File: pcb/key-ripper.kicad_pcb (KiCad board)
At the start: 2 copper layers, 290.5 x 121.4 mm, 193 parts, among them J1 Conn_01x04, SW1 ESC, SW10 F9, SW11 F10, SW12 F11, SW13 F12, SW14 TILDE, SW15 1, SW16 2, SW17 3, SW18 4, SW19 5, SW2 F1, SW20 6, SW21 7, SW22 8, SW23 9, SW24 0, SW25 -, SW26 +, SW27 BACKSPACE, SW28 TAB, SW29 Q, SW3 F2, SW30 W, SW31 E, SW32 R, SW33 T, SW34 Y, SW35 U, SW36 I, SW37 O, SW38 P, SW39 [, SW4 F3, SW40 ], SW41 BACKSLASH, SW42 CAPS, SW43 A, SW44 S, SW45 D, SW46 F, SW47 G, SW48 H, SW49 J, SW5 F4, SW50 K, SW51 L, SW52 ;, SW53 ', SW54 ENTER, SW55 L_SHIFT, SW56 Z, SW57 X, SW58 C, SW59 V, SW6 F5, SW60 B, SW61 N, SW62 M, SW63 ,, SW64 ., SW65 FWD_SLASH, SW66 UP, SW67 FN, SW68 BL_CTRL, SW69 L_ALT, SW7 F6, SW70 L_CMD, SW71 SPACE, SW72 R_CMD, SW73 LEFT, SW74 DOWN, SW75 RIGHT, SW8 F7, SW9 F8, U1 RP2040, U2 TYPE-C-31-M-12, U3 XC6206PxxxMR, U4 W25Q128JVS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

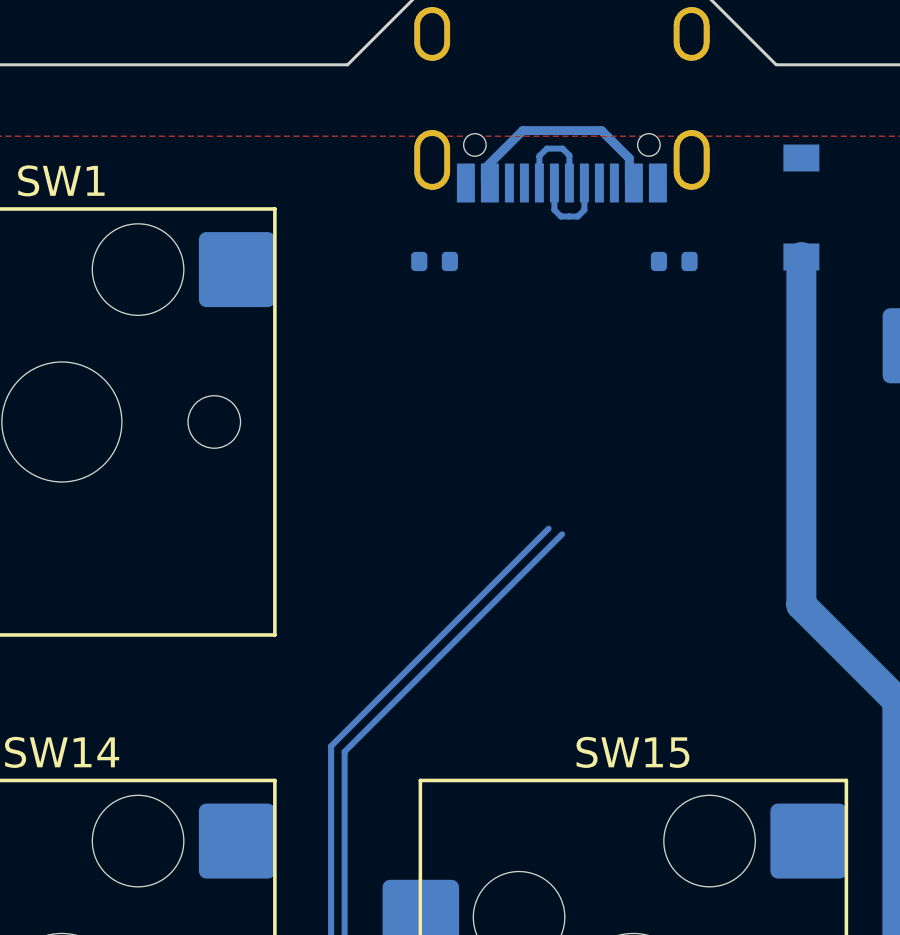
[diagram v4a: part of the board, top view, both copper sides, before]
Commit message: Reattach USB C differential pair
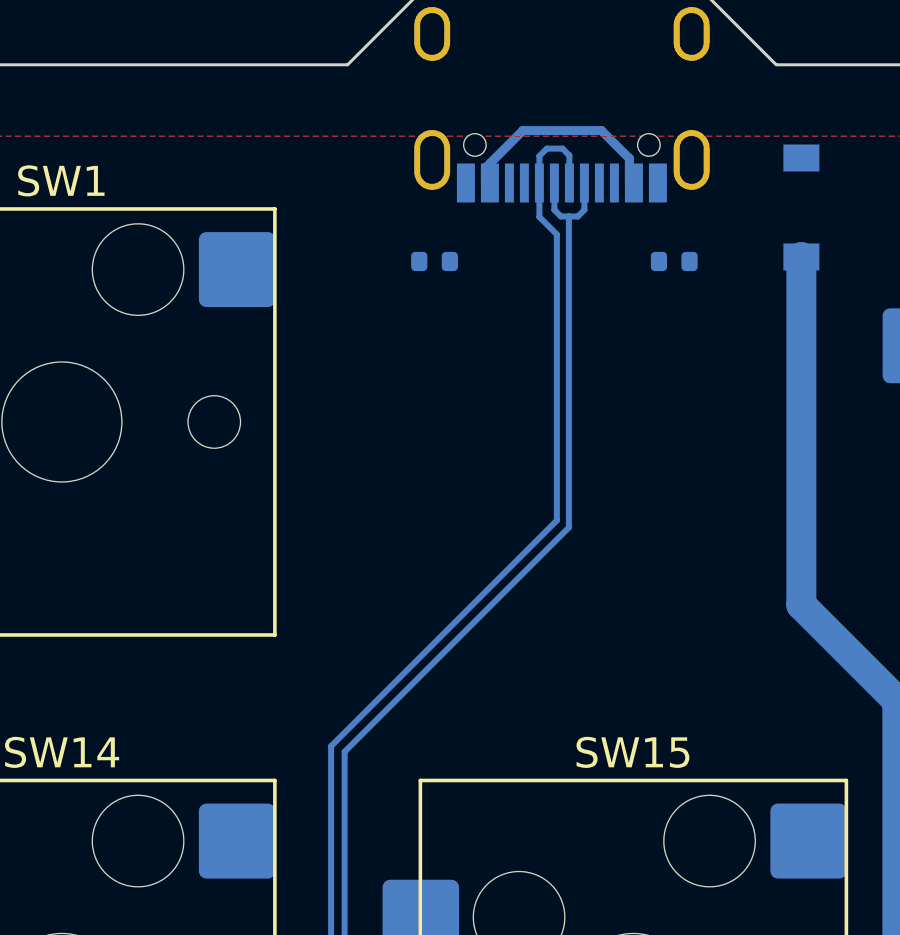
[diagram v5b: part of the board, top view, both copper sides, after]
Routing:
- net USB-: track 173.8 -> 185.6 mm
- net USB+: track 172.8 -> 183.5 mm
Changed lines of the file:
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@@
   (segment (start 18.91767 -27.83233) (end 18.91767 -27.015913) (width 0.3) (layer "B.Cu") (net 94))
   (segment (start 17.417797 -26.117018) (end 17.200779 -25.9) (width 0.2) (layer "B.Cu") (net 100))
+  (segment (start 12.0932 11.225) (end 15.8432 11.225) (width 0.2) (layer "B.Cu") (net 100))
+  (segment (start 16.9 -25.9) (end 16.9 -15.5318) (width 0.2) (layer "B.Cu") (net 100))
+  (segment (start 15.8432 11.225) (end 17.525 12.9068) (width 0.2) (layer "B.Cu") (net 100))
+  (segment (start 9.425 8.5568) (end 12.0932 11.225) (width 0.2) (layer "B.Cu") (net 100))
+  (segment (start 16.9 -15.5318) (end 9.425 -8.0568) (width 0.2) (layer "B.Cu") (net 100))
+  (segment (start 31.1432 47.525) (end 31.675 48.0568) (width 0.2) (layer "B.Cu") (net 100))
   (segment (start 17.525 12.9068) (end 17.525 46.6068) (width 0.2) (layer "B.Cu") (net 100))
-  (segment (start 35.1432 67.875) (end 67.7432 67.875) (width 0.2) (layer "B.Cu") (net 100))
+  (segment (start 17.200779 -25.9) (end 16.9 -25.9) (width 0.2) (layer "B.Cu") (net 100))
   (segment (start 31.675 64.4068) (end 35.1432 67.875) (width 0.2) (layer "B.Cu") (net 100))
-  (segment (start 31.675 48.0568) (end 31.675 64.4068) (width 0.2) (layer "B.Cu") (net 100))
-  (segment (start 12.0932 11.225) (end 15.8432 11.225) (width 0.2) (layer "B.Cu") (net 100))
-  (segment (start 18.4432 47.525) (end 31.1432 47.525) (width 0.2) (layer "B.Cu") (net 100))
-  (segment (start 17.200779 -25.9) (end 16.9 -25.9) (width 0.2) (layer "B.Cu") (net 100))
-  (segment (start 31.1432 47.525) (end 31.675 48.0568) (width 0.2) (layer "B.Cu") (net 100))
-  (segment (start 67.7432 67.875) (end 77.343199 77.474999) (width 0.2) (layer "B.Cu") (net 100))
   (segment (start 94.115001 77.474999) (end 94.39 77.2) (width 0.2) (layer "B.Cu") (net 100))
   (segment (start 16.417797 -26.116764) (end 16.417797 -27.015913) (width 0.2) (layer "B.Cu") (net 100))
-  (segment (start 16.675 -15.3068) (end 9.425 -8.0568) (width 0.2) (layer "B.Cu") (net 100))
-  (segment (start 9.425 8.5568) (end 12.0932 11.225) (width 0.2) (layer "B.Cu") (net 100))
+  (segment (start 9.425 -8.0568) (end 9.425 8.5568) (width 0.2) (layer "B.Cu") (net 100))
+  (segment (start 31.675 48.0568) (end 31.675 64.4068) (width 0.2) (layer "B.Cu") (net 100))
   (segment (start 16.9 -25.9) (end 16.634561 -25.9) (width 0.2) (layer "B.Cu") (net 100))
+  (segment (start 18.4432 47.525) (end 31.1432 47.525) (width 0.2) (layer "B.Cu") (net 100))
   (segment (start 77.343199 77.474999) (end 94.115001 77.474999) (width 0.2) (layer "B.Cu") (net 100))
-  (segment (start 17.525 46.6068) (end 18.4432 47.525) (width 0.2) (layer "B.Cu") (net 100))
-  (segment (start 15.8432 11.225) (end 17.525 12.9068) (width 0.2) (layer "B.Cu") (net 100))
-  (segment (start 9.425 -8.0568) (end 9.425 8.5568) (width 0.2) (layer "B.Cu") (net 100))
+  (segment (start 67.7432 67.875) (end 77.343199 77.474999) (width 0.2) (layer "B.Cu") (net 100))
+  (segment (start 35.1432 67.875) (end 67.7432 67.875) (width 0.2) (layer "B.Cu") (net 100))
   (segment (start 16.634561 -25.9) (end 16.417797 -26.116764) (width 0.2) (layer "B.Cu") (net 100))
   (segment (start 17.417797 -27.015913) (end 17.417797 -26.117018) (width 0.2) (layer "B.Cu") (net 100))
+  (segment (start 17.525 46.6068) (end 18.4432 47.525) (width 0.2) (layer "B.Cu") (net 100))
+  (segment (start 17.075 46.7932) (end 18.2568 47.975) (width 0.2) (layer "B.Cu") (net 101))
   (segment (start 16.6875 -28.1625) (end 16.91767 -27.93233) (width 0.2) (layer "B.Cu") (net 101))
+  (segment (start 16.165362 -28.1625) (end 16.6875 -28.1625) (width 0.2) (layer "B.Cu") (net 101))
+  (segment (start 15.91767 -27.015913) (end 15.91767 -25.88233) (width 0.2) (layer "B.Cu") (net 101))
+  (segment (start 30.9568 47.975) (end 31.225 48.2432) (width 0.2) (layer "B.Cu") (net 101))
+  (segment (start 15.91767 -25.88233) (end 16.5 -25.3) (width 0.2) (layer "B.Cu") (net 101))
+  (segment (start 94.115001 77.925001) (end 94.39 78.2) (width 0.2) (layer "B.Cu") (net 101))
+  (segment (start 16.91767 -27.93233) (end 16.91767 -27.015913) (width 0.2) (layer "B.Cu") (net 101))
+  (segment (start 31.225 64.5932) (end 34.9568 68.325) (width 0.2) (layer "B.Cu") (net 101))
+  (segment (start 77.156801 77.925001) (end 94.115001 77.925001) (width 0.2) (layer "B.Cu") (net 101))
+  (segment (start 16.5 -15.7682) (end 8.975 -8.2432) (width 0.2) (layer "B.Cu") (net 101))
+  (segment (start 34.9568 68.325) (end 67.5568 68.325) (width 0.2) (layer "B.Cu") (net 101))
+  (segment (start 15.91767 -27.914808) (end 16.165362 -28.1625) (width 0.2) (layer "B.Cu") (net 101))
+  (segment (start 67.5568 68.325) (end 77.156801 77.925001) (width 0.2) (layer "B.Cu") (net 101))
   (segment (start 8.975 8.7432) (end 11.9068 11.675) (width 0.2) (layer "B.Cu") (net 101))
-  (segment (start 16.165362 -28.1625) (end 16.6875 -28.1625) (width 0.2) (layer "B.Cu") (net 101))
+  (segment (start 11.9068 11.675) (end 15.6568 11.675) (width 0.2) (layer "B.Cu") (net 101))
+  (segment (start 15.6568 11.675) (end 17.075 13.0932) (width 0.2) (layer "B.Cu") (net 101))
+  (segment (start 15.91767 -27.015913) (end 15.91767 -27.914808) (width 0.2) (layer "B.Cu") (net 101))
   (segment (start 31.225 48.2432) (end 31.225 64.5932) (width 0.2) (layer "B.Cu") (net 101))
-  (segment (start 16.225 -15.4932) (end 8.975 -8.2432) (width 0.2) (layer "B.Cu") (net 101))
-  (segment (start 16.91767 -27.93233) (end 16.91767 -27.015913) (width 0.2) (layer "B.Cu") (net 101))
+  (segment (start 18.2568 47.975) (end 30.9568 47.975) (width 0.2) (layer "B.Cu") (net 101))
   (segment (start 17.075 13.0932) (end 17.075 46.7932) (width 0.2) (layer "B.Cu") (net 101))
-  (segment (start 11.9068 11.675) (end 15.6568 11.675) (width 0.2) (layer "B.Cu") (net 101))
-  (segment (start 15.91767 -27.914808) (end 16.165362 -28.1625) (width 0.2) (layer "B.Cu") (net 101))
-  (segment (start 15.6568 11.675) (end 17.075 13.0932) (width 0.2) (layer "B.Cu") (net 101))
+  (segment (start 16.5 -25.3) (end 16.5 -15.7682) (width 0.2) (layer "B.Cu") (net 101))
   (segment (start 8.975 -8.2432) (end 8.975 8.7432) (width 0.2) (layer "B.Cu") (net 101))
-  (segment (start 17.075 46.7932) (end 18.2568 47.975) (width 0.2) (layer "B.Cu") (net 101))
-  (segment (start 18.2568 47.975) (end 30.9568 47.975) (width 0.2) (layer "B.Cu") (net 101))
-  (segment (start 94.115001 77.925001) (end 94.39 78.2) (width 0.2) (layer "B.Cu") (net 101))
-  (segment (start 31.225 64.5932) (end 34.9568 68.325) (width 0.2) (layer "B.Cu") (net 101))
-  (segment (start 30.9568 47.975) (end 31.225 48.2432) (width 0.2) (layer "B.Cu") (net 101))
-  (segment (start 15.91767 -27.015913) (end 15.91767 -27.914808) (width 0.2) (layer "B.Cu") (net 101))
-  (segment (start 67.5568 68.325) (end 77.156801 77.925001) (width 0.2) (layer "B.Cu") (net 101))
-  (segment (start 34.9568 68.325) (end 67.5568 68.325) (width 0.2) (layer "B.Cu") (net 101))
-  (segment (start 77.156801 77.925001) (end 94.115001 77.925001) (width 0.2) (layer "B.Cu") (net 101))
   (segment (start 96.069911 69.77) (end 92.9 69.77) (width 0.2) (layer "B.Cu") (net 102))
   (segment (start 100.099962 73.800051) (end 96.069911 69.77) (width 0.2) (layer "B.Cu") (net 102))

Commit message: Make the edge cutouts even smaller
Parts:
- moved R6 2.97 mm to (20.4, -21.4)
- moved R7 2.97 mm to (12.4, -21.4)
- moved U2 2.97 mm to (16.7, -27.8)
- turned H2 to 180 degrees
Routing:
- net USB-: track 185.6 -> 182.7 mm
- net USB+: track 183.5 -> 180.7 mm
- net Net-(D76-Pad1): track 188.9 -> 190.0 mm
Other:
- board size 290.5 x 121.4 mm -> 285.8 x 116.7 mm

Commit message: Small adjustments
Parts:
- moved C18 55.7 mm to (91.3, 95.3)
- moved R8 55.7 mm to (102.1, 96.3)
- moved U6 55.7 mm to (96.5, 95.0)
- moved J1 52.5 mm to (112.0, 106.8)
- moved U5 30.9 mm to (119.3, 95.2)
- moved R5 30.9 mm to (113.2, 93.4)
- moved D76 5.40 mm to (24.6, -20.8)
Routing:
- net Net-(D76-Pad1): track 190.0 -> 184.6 mm
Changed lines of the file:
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@@
     (property "Sheetname" "")
     (attr smd)
-    (fp_text reference "C9" (at 1.97 3.8 -270) (layer "B.SilkS")
+    (fp_text reference "C9" (at 1.57 3.8 -270) (layer "B.SilkS")
       (effects (font (size 1 1) (thickness 0.15)) (justify mirror))
     )
@@
   )
   (footprint "Connector_PinHeader_2.54mm:PinHeader_1x04_P2.54mm_Vertical" (layer "B.Cu")
-    (at 164.5 108.3 90)
+    (at 112 106.8 90)
     (descr "Through hole straight pin header, 1x04, 2.54mm pitch, single row")
     (tags "Through hole pin header THT 1x04 2.54mm single row")
@@
     (property "Sheetname" "")
     (attr smd)
-    (fp_text reference "C1" (at 1.95 4.4 -270) (layer "B.SilkS")
+    (fp_text reference "C1" (at 1.55 4.4 -270) (layer "B.SilkS")
       (effects (font (size 1 1) (thickness 0.15)) (justify mirror))
     )
@@
   )
   (footprint "Capacitor_SMD:C_0402_1005Metric" (layer "B.Cu")
-    (at 35.775 99.535 90)
+    (at 91.3 95.27 90)
     (descr "Capacitor SMD 0402 (1005 Metric), square (rectangular) end terminal, IPC_7351 nominal, (Body size source: IPC-SM-782 page 76, https://www.pcb-3d.com/wordpress/wp-content/uploads/ipc-sm-782a_amendment_1_and_2.pdf), generated with kicad-footprint-generator")
     (tags "capacitor")
@@
     (property "Sheetname" "")
     (attr smd)
-    (fp_text reference "FB1" (at 0 -1.675) (layer "B.SilkS")
+    (fp_text reference "FB1" (at 3.2 -0.05) (layer "B.SilkS")
       (effects (font (size 1 1) (thickness 0.15)) (justify mirror))
     )
@@
   )
   (footprint "Diode_SMD:D_SOD-123" (layer "B.Cu")
-    (at 24.65 -26.2 90)
+    (at 24.65 -20.8 90)
     (descr "SOD-123")
     (tags "SOD-123")
@@
   )
   (footprint "Resistor_SMD:R_0402_1005Metric" (layer "B.Cu")
-    (at 46.6 100.6 90)
+    (at 102.125 96.335 90)
     (descr "Resistor SMD 0402 (1005 Metric), square (rectangular) end terminal, IPC_7351 nominal, (Body size source: IPC-SM-782 page 72, https://www.pcb-3d.com/wordpress/wp-content/uploads/ipc-sm-782a_amendment_1_and_2.pdf), generated with kicad-footprint-generator")
     (tags "resistor")
@@
   )
   (footprint "footprints:tactile-switch" (layer "B.Cu")
-    (at 40.975 99.265 180)
+    (at 96.5 95 180)
     (descr "SW-SMD_4P-L5.1-W5.1-P3.70-LS6.5-TL-2 footprint")
     (tags "SW-SMD_4P-L5.1-W5.1-P3.70-LS6.5-TL-2 footprint")
@@
     (property "Sheetname" "")
     (attr smd)
-    (fp_text reference "R4" (at 0 1.17) (layer "B.SilkS")
+    (fp_text reference "R4" (at 2 0) (layer "B.SilkS")
       (effects (font (size 1 1) (thickness 0.15)) (justify mirror))
     )
@@
   )
   (footprint "Resistor_SMD:R_0402_1005Metric" (layer "B.Cu")
-    (at 143.7 88.6)
+    (at 113.2 93.4)
     (descr "Resistor SMD 0402 (1005 Metric), square (rectangular) end terminal, IPC_7351 nominal, (Body size source: IPC-SM-782 page 72, https://www.pcb-3d.com/wordpress/wp-content/uploads/ipc-sm-782a_amendment_1_and_2.pdf), generated with kicad-footprint-generator")
     (tags "resistor")
@@
     (property "Sheetname" "")
     (attr smd)
-    (fp_text reference "C15" (at 2.37 3.3 -270) (layer "B.SilkS")
+    (fp_text reference "C15" (at 1.97 3.3 -270) (layer "B.SilkS")
       (effects (font (size 1 1) (thickness 0.15)) (justify mirror))
     )
@@
   )
   (footprint "footprints:tactile-switch" (layer "B.Cu")
-    (at 149.8 90.4)
+    (at 119.3 95.2)
     (descr "SW-SMD_4P-L5.1-W5.1-P3.70-LS6.5-TL-2 footprint")
     (tags "SW-SMD_4P-L5.1-W5.1-P3.70-LS6.5-TL-2 footprint")
@@
   (segment (start 103.899975 72.849835) (end 103.899975 69.114013) (width 0.2) (layer "B.Cu") (net 81))
   (segment (start 103.899975 69.114013) (end 103.948945 69.065043) (width 0.2) (layer "B.Cu") (net 81))
+  (segment (start 24.65 -19.15) (end 24.65 -12.95) (width 1) (layer "B.Cu") (net 89))
+  (segment (start 52.1 50.15) (end 52.1 65.05) (width 1) (layer "B.Cu") (net 89))
+  (segment (start 24.65 -12.95) (end 27.85 -9.75) (width 1) (layer "B.Cu") (net 89))
   (segment (start 116.65 65.7) (end 121.3 70.35) (width 1) (layer "B.Cu") (net 89))
-  (segment (start 34.95 9) (end 37.65 11.7) (width 1) (layer "B.Cu") (net 89))
-  (segment (start 29.65 9) (end 34.95 9) (width 1) (layer "B.Cu") (net 89))
-  (segment (start 44.15 48) (end 49.95 48) (width 1) (layer "B.Cu") (net 89))
-  (segment (start 82.8 64.3) (end 84.2 65.7) (width 1) (layer "B.Cu") (net 89))
-  (segment (start 27.85 -9.75) (end 27.85 7.2) (width 1) (layer "B.Cu") (net 89))
   (segment (start 77.8 65.6) (end 79.1 64.3) (width 1) (layer "B.Cu") (net 89))
-  (segment (start 24.65 -24.55) (end 24.65 -12.95) (width 1) (layer "B.Cu") (net 89))
-  (segment (start 24.65 -12.95) (end 27.85 -9.75) (width 1) (layer "B.Cu") (net 89))
-  (segment (start 52.1 50.15) (end 52.1 65.05) (width 1) (layer "B.Cu") (net 89))
+  (segment (start 82.8 64.3) (end 84.2 65.7) (width 1) (layer "B.Cu") (net 89))
   (segment (start 52.1 65.05) (end 52.65 65.6) (width 1) (layer "B.Cu") (net 89))
-  (segment (start 37.65 26.2) (end 42.35 30.9) (width 1) (layer "B.Cu") (net 89))
-  (segment (start 27.85 7.2) (end 29.65 9) (width 1) (layer "B.Cu") (net 89))
   (segment (start 121.3 70.35) (end 121.3 80.4125) (width 1) (layer "B.Cu") (net 89))
-  (segment (start 37.65 11.7) (end 37.65 26.2) (width 1) (layer "B.Cu") (net 89))
-  (segment (start 49.95 48) (end 52.1 50.15) (width 1) (layer "B.Cu") (net 89))
+  (segment (start 27.85 7.2) (end 29.65 9) (width 1) (layer "B.Cu") (net 89))
+  (segment (start 37.65 26.2) (end 42.35 30.9) (width 1) (layer "B.Cu") (net 89))
+  (segment (start 42.35 46.2) (end 44.15 48) (width 1) (layer "B.Cu") (net 89))
+  (segment (start 42.35 30.9) (end 42.35 46.2) (width 1) (layer "B.Cu") (net 89))
+  (segment (start 27.85 -9.75) (end 27.85 7.2) (width 1) (layer "B.Cu") (net 89))
   (segment (start 52.65 65.6) (end 77.8 65.6) (width 1) (layer "B.Cu") (net 89))
+  (segment (start 34.95 9) (end 37.65 11.7) (width 1) (layer "B.Cu") (net 89))
+  (segment (start 29.65 9) (end 34.95 9) (width 1) (layer "B.Cu") (net 89))
   (segment (start 79.1 64.3) (end 82.8 64.3) (width 1) (layer "B.Cu") (net 89))
-  (segment (start 42.35 30.9) (end 42.35 46.2) (width 1) (layer "B.Cu") (net 89))
+  (segment (start 49.95 48) (end 52.1 50.15) (width 1) (layer "B.Cu") (net 89))
+  (segment (start 37.65 11.7) (end 37.65 26.2) (width 1) (layer "B.Cu") (net 89))
   (segment (start 84.2 65.7) (end 116.65 65.7) (width 1) (layer "B.Cu") (net 89))
-  (segment (start 42.35 46.2) (end 44.15 48) (width 1) (layer "B.Cu") (net 89))
+  (segment (start 44.15 48) (end 49.95 48) (width 1) (layer "B.Cu") (net 89))
   (segment (start 95.61 77.4) (end 95.41 77.2) (width 0.2) (layer "B.Cu") (net 92))
   (segment (start 100.549962 77.4) (end 95.61 77.4) (width 0.2) (layer "B.Cu") (net 92))

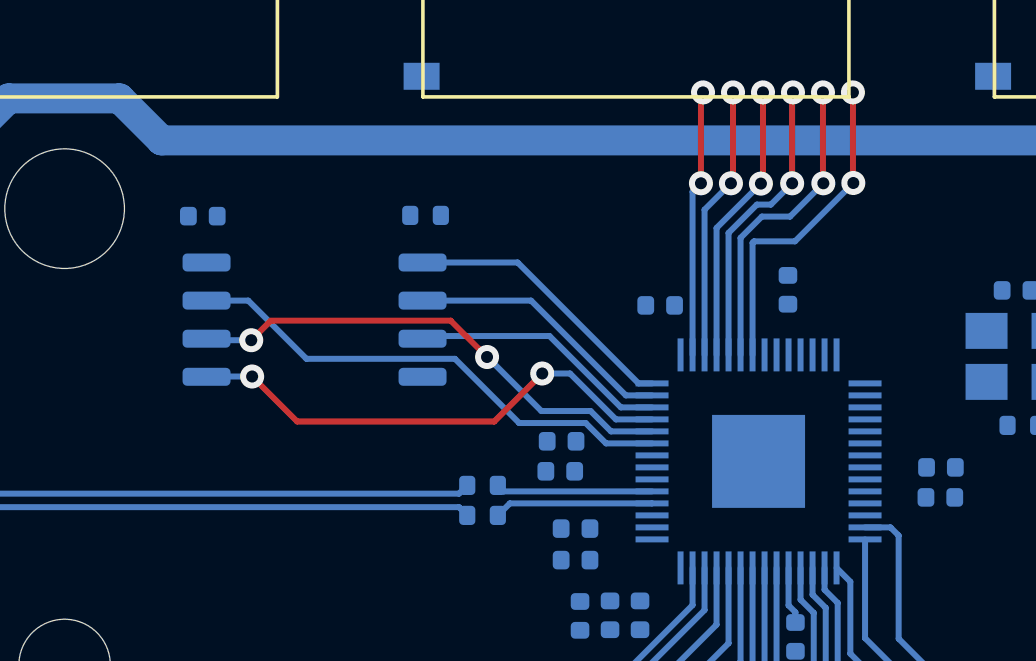
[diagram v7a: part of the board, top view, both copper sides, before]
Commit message: Move QSPI flash closer to the RP2040
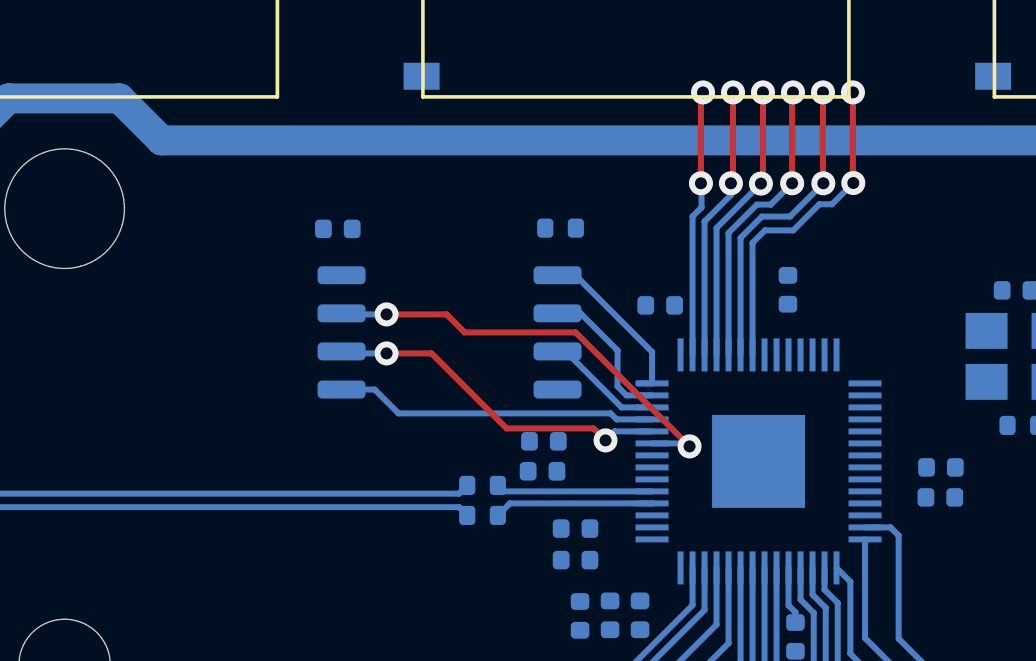
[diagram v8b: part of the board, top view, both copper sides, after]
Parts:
- moved C3 4.52 mm to (90.1, 68.7)
- moved R4 4.52 mm to (97.5, 68.6)
- moved U4 4.52 mm to (93.8, 72.1)
- moved C16 0.59 mm to (96.9, 75.7)
- moved C14 0.59 mm to (96.9, 76.7)
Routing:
- net QSPI_SD0: track 16.8 -> 10.8 mm, vias 2 -> 0
- net QSPI_SCLK: track 16.7 -> 11.7 mm
- net QSPI_SD2: track 8.67 -> 3.92 mm
- net QSPI_SD1: track 8.96 -> 4.99 mm
- net QSPI_SS: track 9.32 -> 5.71 mm
- net QSPI_SD3: track 16.8 -> 14.7 mm, vias 0 -> 2
